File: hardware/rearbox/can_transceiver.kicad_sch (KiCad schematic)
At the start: 9 parts

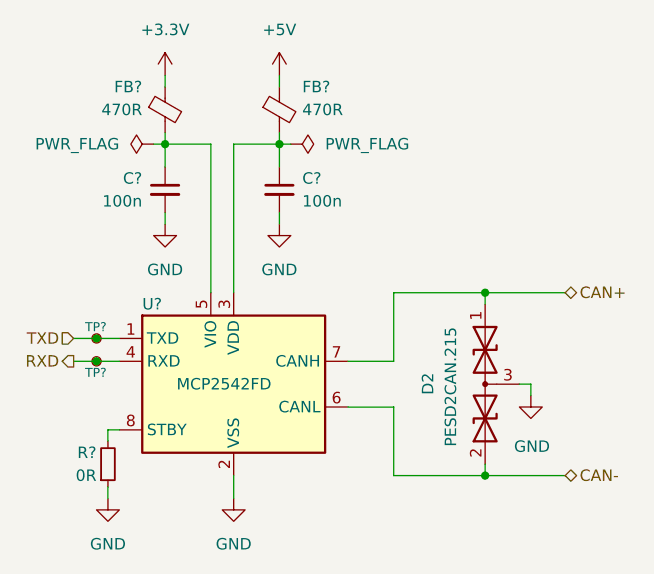
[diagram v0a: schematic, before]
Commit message: Place components on the PCB
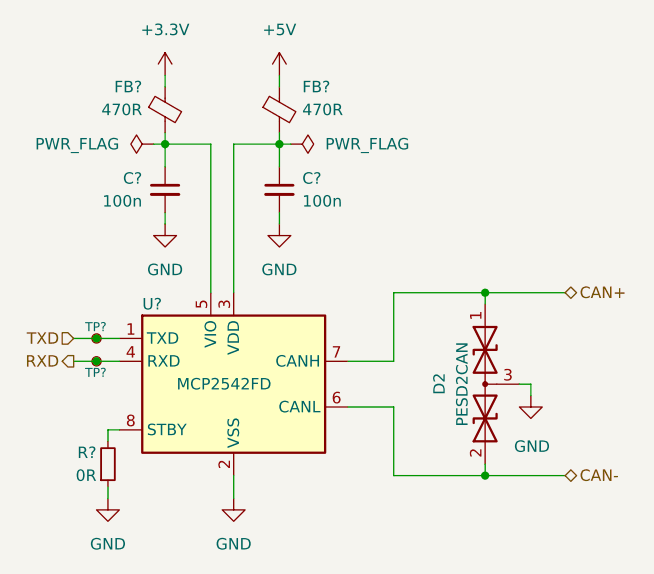
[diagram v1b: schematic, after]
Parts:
- D2: value PESD2CAN.215 -> PESD2CAN
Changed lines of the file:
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@@
   (title_block
     (title "CAN Transceiver")
-    (date "2023-10-01")
+    (date "2023-11-02")
     (rev "${REVISION}")
     (company "Author: I. Kajdan")
@@
   (symbol (lib_id "Device:D_TVS_Dual_AAC") (at 168.91 107.95 90) (mirror x) (unit 1)
     (in_bom yes) (on_board yes) (dnp no)
-    (property "Reference" "D2" (at 162.56 106.68 0)
-      (effects (font (size 1.27 1.27)) (justify left))
-    )
-    (property "Value" "PESD2CAN.215" (at 165.1 101.6 0)
-      (effects (font (size 1.27 1.27)) (justify left))
+    (property "Reference" "D2" (at 163.83 106.68 0)
+      (effects (font (size 1.27 1.27)) (justify left))
+    )
+    (property "Value" "PESD2CAN" (at 166.37 107.95 0)
+      (effects (font (size 1.27 1.27)))
     )
     (property "Footprint" "Package_TO_SOT_SMD:SOT-23" (at 168.91 104.14 0)
@@
         )
         (path "/b652b05a-4e3d-4ad1-b032-18886abe7d45/38408e41-dfb1-4c27-acb0-3f1224cc8789/eec2c93a-0fce-4d3a-ab43-9e1e0481c06c"
-          (reference "C27") (unit 1)
-        )
-        (path "/b652b05a-4e3d-4ad1-b032-18886abe7d45/38408e41-dfb1-4c27-acb0-3f1224cc8789/f1ed15a3-9302-436f-b25a-713477aeadf3"
-          (reference "C29") (unit 1)
+          (reference "C26") (unit 1)
+        )
+        (path "/b652b05a-4e3d-4ad1-b032-18886abe7d45/38408e41-dfb1-4c27-acb0-3f1224cc8789/f1ed15a3-9302-436f-b25a-713477aeadf3"
+          (reference "C28") (unit 1)
         )
       )
@@
         )
         (path "/b652b05a-4e3d-4ad1-b032-18886abe7d45/38408e41-dfb1-4c27-acb0-3f1224cc8789/eec2c93a-0fce-4d3a-ab43-9e1e0481c06c"
-          (reference "TP11") (unit 1)
-        )
-        (path "/b652b05a-4e3d-4ad1-b032-18886abe7d45/38408e41-dfb1-4c27-acb0-3f1224cc8789/f1ed15a3-9302-436f-b25a-713477aeadf3"
-          (reference "TP13") (unit 1)
+          (reference "TP12") (unit 1)
+        )
+        (path "/b652b05a-4e3d-4ad1-b032-18886abe7d45/38408e41-dfb1-4c27-acb0-3f1224cc8789/f1ed15a3-9302-436f-b25a-713477aeadf3"
+          (reference "TP14") (unit 1)
         )
       )
@@
         )
         (path "/b652b05a-4e3d-4ad1-b032-18886abe7d45/38408e41-dfb1-4c27-acb0-3f1224cc8789/eec2c93a-0fce-4d3a-ab43-9e1e0481c06c"
-          (reference "#PWR059") (unit 1)
-        )
-        (path "/b652b05a-4e3d-4ad1-b032-18886abe7d45/38408e41-dfb1-4c27-acb0-3f1224cc8789/f1ed15a3-9302-436f-b25a-713477aeadf3"
-          (reference "#PWR065") (unit 1)
+          (reference "#PWR058") (unit 1)
+        )
+        (path "/b652b05a-4e3d-4ad1-b032-18886abe7d45/38408e41-dfb1-4c27-acb0-3f1224cc8789/f1ed15a3-9302-436f-b25a-713477aeadf3"
+          (reference "#PWR064") (unit 1)
         )
       )
@@
         )
         (path "/b652b05a-4e3d-4ad1-b032-18886abe7d45/38408e41-dfb1-4c27-acb0-3f1224cc8789/eec2c93a-0fce-4d3a-ab43-9e1e0481c06c"
-          (reference "#PWR061") (unit 1)
-        )
-        (path "/b652b05a-4e3d-4ad1-b032-18886abe7d45/38408e41-dfb1-4c27-acb0-3f1224cc8789/f1ed15a3-9302-436f-b25a-713477aeadf3"
-          (reference "#PWR067") (unit 1)
+          (reference "#PWR060") (unit 1)
+        )
+        (path "/b652b05a-4e3d-4ad1-b032-18886abe7d45/38408e41-dfb1-4c27-acb0-3f1224cc8789/f1ed15a3-9302-436f-b25a-713477aeadf3"
+          (reference "#PWR066") (unit 1)
         )
       )
@@
         )
         (path "/b652b05a-4e3d-4ad1-b032-18886abe7d45/38408e41-dfb1-4c27-acb0-3f1224cc8789/eec2c93a-0fce-4d3a-ab43-9e1e0481c06c"
-          (reference "TP12") (unit 1)
-        )
-        (path "/b652b05a-4e3d-4ad1-b032-18886abe7d45/38408e41-dfb1-4c27-acb0-3f1224cc8789/f1ed15a3-9302-436f-b25a-713477aeadf3"
-          (reference "TP14") (unit 1)
+          (reference "TP13") (unit 1)
+        )
+        (path "/b652b05a-4e3d-4ad1-b032-18886abe7d45/38408e41-dfb1-4c27-acb0-3f1224cc8789/f1ed15a3-9302-436f-b25a-713477aeadf3"
+          (reference "TP15") (unit 1)
         )
       )
@@
         )
         (path "/b652b05a-4e3d-4ad1-b032-18886abe7d45/38408e41-dfb1-4c27-acb0-3f1224cc8789/eec2c93a-0fce-4d3a-ab43-9e1e0481c06c"
-          (reference "#PWR060") (unit 1)
-        )
-        (path "/b652b05a-4e3d-4ad1-b032-18886abe7d45/38408e41-dfb1-4c27-acb0-3f1224cc8789/f1ed15a3-9302-436f-b25a-713477aeadf3"
-          (reference "#PWR066") (unit 1)
+          (reference "#PWR059") (unit 1)
+        )
+        (path "/b652b05a-4e3d-4ad1-b032-18886abe7d45/38408e41-dfb1-4c27-acb0-3f1224cc8789/f1ed15a3-9302-436f-b25a-713477aeadf3"
+          (reference "#PWR065") (unit 1)
         )
       )
@@
   (symbol (lib_id "power:+5V") (at 146.05 73.66 0) (unit 1)
     (in_bom yes) (on_board yes) (dnp no) (fields_autoplaced)
-    (property "Reference" "#PWR062" (at 146.05 77.47 0)
+    (property "Reference" "#PWR061" (at 146.05 77.47 0)
       (effects (font (size 1.27 1.27)) hide)
     )
@@
       (project "rearbox"
         (path "/b652b05a-4e3d-4ad1-b032-18886abe7d45/38408e41-dfb1-4c27-acb0-3f1224cc8789/eec2c93a-0fce-4d3a-ab43-9e1e0481c06c"
-          (reference "#PWR062") (unit 1)
-        )
-        (path "/b652b05a-4e3d-4ad1-b032-18886abe7d45/38408e41-dfb1-4c27-acb0-3f1224cc8789/f1ed15a3-9302-436f-b25a-713477aeadf3"
-          (reference "#PWR068") (unit 1)
+          (reference "#PWR061") (unit 1)
+        )
+        (path "/b652b05a-4e3d-4ad1-b032-18886abe7d45/38408e41-dfb1-4c27-acb0-3f1224cc8789/f1ed15a3-9302-436f-b25a-713477aeadf3"
+          (reference "#PWR067") (unit 1)
         )
       )
@@
         )
         (path "/b652b05a-4e3d-4ad1-b032-18886abe7d45/38408e41-dfb1-4c27-acb0-3f1224cc8789/eec2c93a-0fce-4d3a-ab43-9e1e0481c06c"
-          (reference "C28") (unit 1)
-        )
-        (path "/b652b05a-4e3d-4ad1-b032-18886abe7d45/38408e41-dfb1-4c27-acb0-3f1224cc8789/f1ed15a3-9302-436f-b25a-713477aeadf3"
-          (reference "C30") (unit 1)
+          (reference "C27") (unit 1)
+        )
+        (path "/b652b05a-4e3d-4ad1-b032-18886abe7d45/38408e41-dfb1-4c27-acb0-3f1224cc8789/f1ed15a3-9302-436f-b25a-713477aeadf3"
+          (reference "C29") (unit 1)
         )
       )
@@
         )
         (path "/b652b05a-4e3d-4ad1-b032-18886abe7d45/38408e41-dfb1-4c27-acb0-3f1224cc8789/eec2c93a-0fce-4d3a-ab43-9e1e0481c06c"
+          (reference "#PWR062") (unit 1)
+        )
+        (path "/b652b05a-4e3d-4ad1-b032-18886abe7d45/38408e41-dfb1-4c27-acb0-3f1224cc8789/f1ed15a3-9302-436f-b25a-713477aeadf3"
+          (reference "#PWR068") (unit 1)
+        )
+      )
+    )
+  )
+  (symbol (lib_id "power:GND") (at 127 120.65 0) (unit 1)
+    (in_bom yes) (on_board yes) (dnp no)
+    (property "Reference" "#PWR?" (at 127 127 0)
+      (effects (font (size 1.27 1.27)) hide)
+    )
+    (property "Value" "GND" (at 127 125.73 0)
+      (effects (font (size 1.27 1.27)))
+    )
+    (property "Footprint" "" (at 127 120.65 0)
+      (effects (font (size 1.27 1.27)) hide)
+    )
+    (property "Datasheet" "" (at 127 120.65 0)
+      (effects (font (size 1.27 1.27)) hide)
+    )
+    (pin "1")
+    (instances
+      (project "rearbox"
+        (path "/b652b05a-4e3d-4ad1-b032-18886abe7d45/38408e41-dfb1-4c27-acb0-3f1224cc8789"
+          (reference "#PWR?") (unit 1)
+        )
+        (path "/b652b05a-4e3d-4ad1-b032-18886abe7d45/38408e41-dfb1-4c27-acb0-3f1224cc8789/eec2c93a-0fce-4d3a-ab43-9e1e0481c06c"
+          (reference "#PWR057") (unit 1)
+        )
+        (path "/b652b05a-4e3d-4ad1-b032-18886abe7d45/38408e41-dfb1-4c27-acb0-3f1224cc8789/f1ed15a3-9302-436f-b25a-713477aeadf3"
           (reference "#PWR063") (unit 1)
-        )
-        (path "/b652b05a-4e3d-4ad1-b032-18886abe7d45/38408e41-dfb1-4c27-acb0-3f1224cc8789/f1ed15a3-9302-436f-b25a-713477aeadf3"
-          (reference "#PWR069") (unit 1)
-        )
-      )
-    )
-  )
-  (symbol (lib_id "power:GND") (at 127 120.65 0) (unit 1)
-    (in_bom yes) (on_board yes) (dnp no)
-    (property "Reference" "#PWR?" (at 127 127 0)
-      (effects (font (size 1.27 1.27)) hide)
-    )
-    (property "Value" "GND" (at 127 125.73 0)
-      (effects (font (size 1.27 1.27)))
-    )
-    (property "Footprint" "" (at 127 120.65 0)
-      (effects (font (size 1.27 1.27)) hide)
-    )
-    (property "Datasheet" "" (at 127 120.65 0)
-      (effects (font (size 1.27 1.27)) hide)
-    )
-    (pin "1")
-    (instances
-      (project "rearbox"
-        (path "/b652b05a-4e3d-4ad1-b032-18886abe7d45/38408e41-dfb1-4c27-acb0-3f1224cc8789"
-          (reference "#PWR?") (unit 1)
-        )
-        (path "/b652b05a-4e3d-4ad1-b032-18886abe7d45/38408e41-dfb1-4c27-acb0-3f1224cc8789/eec2c93a-0fce-4d3a-ab43-9e1e0481c06c"
-          (reference "#PWR058") (unit 1)
-        )
-        (path "/b652b05a-4e3d-4ad1-b032-18886abe7d45/38408e41-dfb1-4c27-acb0-3f1224cc8789/f1ed15a3-9302-436f-b25a-713477aeadf3"
-          (reference "#PWR064") (unit 1)
         )
       )
@@
         )
         (path "/b652b05a-4e3d-4ad1-b032-18886abe7d45/38408e41-dfb1-4c27-acb0-3f1224cc8789/f1ed15a3-9302-436f-b25a-713477aeadf3"
-          (reference "R11") (unit 1)
-        )
-        (path "/b652b05a-4e3d-4ad1-b032-18886abe7d45/38408e41-dfb1-4c27-acb0-3f1224cc8789/eec2c93a-0fce-4d3a-ab43-9e1e0481c06c"
-          (reference "R10") (unit 1)
-        )
-      )
+          (reference "R7") (unit 1)
+        )
+        (path "/b652b05a-4e3d-4ad1-b032-18886abe7d45/38408e41-dfb1-4c27-acb0-3f1224cc8789/eec2c93a-0fce-4d3a-ab43-9e1e0481c06c"
+          (reference "R6") (unit 1)
+        )
+      )

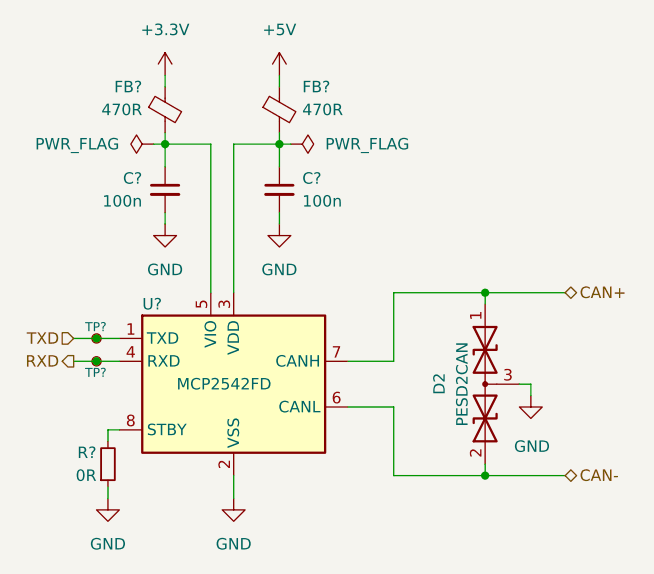
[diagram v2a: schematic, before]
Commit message: Route PCB tracks
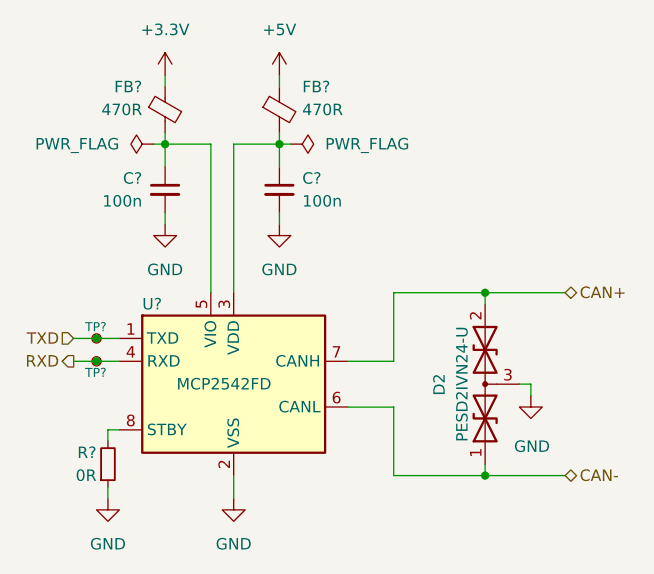
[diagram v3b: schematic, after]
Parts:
- D2: value PESD2CAN -> PESD2IVN24-U; footprint Package_TO_SOT_SMD:SOT-23 -> Package_TO_SOT_SMD:SOT-323_SC-70
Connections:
- net CAN+: now also D2.2 (A2); no longer D2.1 (A1)
- net CAN-: now also D2.1 (A1); no longer D2.2 (A2)
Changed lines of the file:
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@@
     )
   )
-  (symbol (lib_id "Device:D_TVS_Dual_AAC") (at 168.91 107.95 90) (mirror x) (unit 1)
+  (symbol (lib_id "Device:D_TVS_Dual_AAC") (at 168.91 107.95 90) (unit 1)
     (in_bom yes) (on_board yes) (dnp no)
-    (property "Reference" "D2" (at 163.83 106.68 0)
+    (property "Reference" "D2" (at 163.83 109.22 0)
       (effects (font (size 1.27 1.27)) (justify left))
     )
-    (property "Value" "PESD2CAN" (at 166.37 107.95 0)
+    (property "Value" "PESD2IVN24-U" (at 166.37 107.95 0)
       (effects (font (size 1.27 1.27)))
     )
-    (property "Footprint" "Package_TO_SOT_SMD:SOT-23" (at 168.91 104.14 0)
+    (property "Footprint" "Package_TO_SOT_SMD:SOT-323_SC-70" (at 168.91 111.76 0)
       (effects (font (size 1.27 1.27)) hide)
     )
-    (property "Datasheet" "https://pl.mouser.com/datasheet/2/916/PESD2CAN-1320343.pdf" (at 168.91 104.14 0)
+    (property "Datasheet" "https://www.mouser.pl/datasheet/2/916/PESD2IVN24_U-1318740.pdf" (at 168.91 111.76 0)
       (effects (font (size 1.27 1.27)) hide)
     )
